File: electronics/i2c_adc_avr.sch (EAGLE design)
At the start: 17 parts, among them IC1 TINY24/44/84-MU, IC2 TINY25/45/85-20MU

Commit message: Rev 0.3 as built (version is mislabeled on silk)
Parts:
- removed IC2: TINY25/45/85-20MU, mes_avr:TINY25/45/85-20MU
- C3: value 1uF -> 0.001uF
- JP5: value (none) -> MISO
- JP6: value (none) -> RESET
- JP7: value (none) -> MCU
- JP8: value (none) -> SIG
- R4: value 10 -> 10K
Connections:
- net !RESET: no longer IC2.(PCINT5/RESET/ADC0/DW)PB5
- net A0: no longer IC2.(MISO/DO/AIN1/OC0B/OC1A/PCINT1)PB1
- net A1: no longer IC2.(PCINT4/XTAL2/CLKO/OC1B/ADC2)PB3
- net AIN: no longer IC2.(PCINT3/XTAL1/CLKI/OC1B/ADC3)PB4
- net GND: now also IC1.GNDPAD
- net SCL: no longer IC2.(SCK/USCK/SCL/ADC1/T0/INT0/PCINT2)PB2
- net SDA: no longer IC2.(MOSI/DI/SDA/AIN0/OC0A/OC1A/AREF/PCINT0)PB0
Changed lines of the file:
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@@
 <part name="P+1" library="supply1" deviceset="VCC" device=""/>
 <part name="SUPPLY1" library="supply2" deviceset="GND" device=""/>
-<part name="C3" library="rcl" deviceset="C-US" device="C0603" value="1uF"/>
+<part name="C3" library="rcl" deviceset="C-US" device="C0603" value="0.001uF"/>
 <part name="C2" library="rcl" deviceset="C-US" device="C0603" value="0.1uF"/>
-<part name="R4" library="rcl" deviceset="R-US_" device="R0603" value="10"/>
+<part name="R4" library="rcl" deviceset="R-US_" device="R0603" value="10K"/>
 <part name="FRAME1" library="mes" deviceset="LETTER_L" device=""/>
 <part name="A0" library="SparkFun" deviceset="SOLDERJUMPER_2WAY" device="S" value=" "/>
@@
 <part name="P+2" library="supply1" deviceset="VCC" device=""/>
 <part name="SUPPLY2" library="supply2" deviceset="GND" device=""/>
-<part name="JP5" library="pinhead-2" deviceset="PINHD-1X01" device="_2.54"/>
-<part name="JP6" library="pinhead-2" deviceset="PINHD-1X01" device="_2.54"/>
-<part name="JP7" library="pinhead-2" deviceset="PINHD-1X04" device="_2.54-S"/>
-<part name="JP8" library="pinhead-2" deviceset="PINHD-1X03" device="_2.00"/>
+<part name="JP5" library="pinhead-2" deviceset="PINHD-1X01" device="_2.54" value="MISO"/>
+<part name="JP6" library="pinhead-2" deviceset="PINHD-1X01" device="_2.54" value="RESET"/>
+<part name="JP7" library="pinhead-2" deviceset="PINHD-1X04" device="_2.54-S" value="MCU"/>
+<part name="JP8" library="pinhead-2" deviceset="PINHD-1X03" device="_2.00" value="SIG"/>
 <part name="SUPPLY6" library="supply2" deviceset="GND" device=""/>
-<part name="IC2" library="mes_avr" deviceset="TINY25/45/85" device="-20MU"/>
 </parts>
 <sheets>
@@
 <instances>
 <instance part="A1" gate="G$1" x="165.1" y="106.68" rot="MR180"/>
-<instance part="P+1" gate="VCC" x="63.5" y="154.94"/>
-<instance part="SUPPLY1" gate="GND" x="63.5" y="121.92"/>
+<instance part="P+1" gate="VCC" x="63.5" y="152.4"/>
+<instance part="SUPPLY1" gate="GND" x="63.5" y="127"/>
 <instance part="C3" gate="G$1" x="58.42" y="35.56"/>
 <instance part="C2" gate="G$1" x="50.8" y="139.7"/>
@@
 <instance part="JP8" gate="A" x="99.06" y="40.64"/>
 <instance part="SUPPLY6" gate="GND" x="76.2" y="20.32"/>
-<instance part="IC2" gate="1" x="187.96" y="147.32"/>
 </instances>
 <busses>
@@
 <label x="134.62" y="149.86" size="1.778" layer="95" rot="MR0"/>
 </segment>
-<segment>
-<pinref part="IC2" gate="1" pin="(PCINT3/XTAL1/CLKI/OC1B/ADC3)PB4"/>
-<wire x1="223.52" y1="152.4" x2="236.22" y2="152.4" width="0.1524" layer="91"/>
-<label x="236.22" y="152.4" size="1.778" layer="95"/>
-</segment>
 </net>
 <net name="SCL" class="0">
@@
 <pinref part="JP7" gate="A" pin="2"/>
 </segment>
-<segment>
-<pinref part="IC2" gate="1" pin="(SCK/USCK/SCL/ADC1/T0/INT0/PCINT2)PB2"/>
-<wire x1="223.52" y1="147.32" x2="236.22" y2="147.32" width="0.1524" layer="91"/>
-<label x="236.22" y="147.32" size="1.778" layer="95"/>
-</segment>
 </net>
 <net name="SDA" class="0">
@@
 <wire x1="127" y1="83.82" x2="99.06" y2="83.82" width="0.1524" layer="91"/>
 <pinref part="JP7" gate="A" pin="3"/>
-</segment>
-<segment>
-<pinref part="IC2" gate="1" pin="(MOSI/DI/SDA/AIN0/OC0A/OC1A/AREF/PCINT0)PB0"/>
-<wire x1="223.52" y1="142.24" x2="236.22" y2="142.24" width="0.1524" layer="91"/>
-<label x="236.22" y="142.24" size="1.778" layer="95"/>
 </segment>
 </net>
@@
 <wire x1="66.04" y1="144.78" x2="63.5" y2="144.78" width="0.1524" layer="91"/>
 <wire x1="63.5" y1="144.78" x2="63.5" y2="147.32" width="0.1524" layer="91"/>
-<wire x1="63.5" y1="147.32" x2="63.5" y2="152.4" width="0.1524" layer="91"/>
+<wire x1="63.5" y1="147.32" x2="63.5" y2="149.86" width="0.1524" layer="91"/>
 <junction x="63.5" y="147.32"/>
 <junction x="63.5" y="147.32"/>
@@
 <segment>
 <wire x1="66.04" y1="132.08" x2="63.5" y2="132.08" width="0.1524" layer="91"/>
-<wire x1="63.5" y1="132.08" x2="63.5" y2="129.54" width="0.1524" layer="91"/>
 <pinref part="SUPPLY1" gate="GND" pin="GND"/>
-<wire x1="63.5" y1="124.46" x2="63.5" y2="129.54" width="0.1524" layer="91"/>
-<junction x="63.5" y="129.54"/>
-<junction x="63.5" y="129.54"/>
-<wire x1="50.8" y1="129.54" x2="63.5" y2="129.54" width="0.1524" layer="91"/>
+<wire x1="63.5" y1="129.54" x2="63.5" y2="132.08" width="0.1524" layer="91"/>
+<junction x="63.5" y="132.08"/>
+<junction x="63.5" y="132.08"/>
+<wire x1="50.8" y1="132.08" x2="63.5" y2="132.08" width="0.1524" layer="91"/>
 <pinref part="C2" gate="G$1" pin="2"/>
-<wire x1="50.8" y1="134.62" x2="50.8" y2="129.54" width="0.1524" layer="91"/>
+<wire x1="50.8" y1="134.62" x2="50.8" y2="132.08" width="0.1524" layer="91"/>
 <pinref part="IC1" gate="1" pin="GND"/>
+<pinref part="IC1" gate="1" pin="GNDPAD"/>
+<wire x1="66.04" y1="137.16" x2="63.5" y2="137.16" width="0.1524" layer="91"/>
+<wire x1="63.5" y1="137.16" x2="63.5" y2="132.08" width="0.1524" layer="91"/>
 </segment>
 <segment>
@@
 <label x="134.62" y="132.08" size="1.778" layer="95" rot="MR0"/>
 </segment>
-<segment>
-<pinref part="IC2" gate="1" pin="(MISO/DO/AIN1/OC0B/OC1A/PCINT1)PB1"/>
-<wire x1="223.52" y1="144.78" x2="236.22" y2="144.78" width="0.1524" layer="91"/>
-<label x="236.22" y="144.78" size="1.778" layer="95"/>
-</segment>
 </net>
 <net name="A1" class="0">
@@
 <label x="134.62" y="134.62" size="1.778" layer="95" rot="MR0"/>
 </segment>
-<segment>
-<pinref part="IC2" gate="1" pin="(PCINT4/XTAL2/CLKO/OC1B/ADC2)PB3"/>
-<wire x1="223.52" y1="149.86" x2="236.22" y2="149.86" width="0.1524" layer="91"/>
-<label x="236.22" y="149.86" size="1.778" layer="95"/>
-</segment>
 </net>
 <net name="!RESET" class="0">
@@
 <pinref part="JP6" gate="A" pin="1"/>
 </segment>
-<segment>
-<pinref part="IC2" gate="1" pin="(PCINT5/RESET/ADC0/DW)PB5"/>
-<wire x1="223.52" y1="154.94" x2="236.22" y2="154.94" width="0.1524" layer="91"/>
-<label x="236.22" y="154.94" size="1.778" layer="95"/>
-</segment>
-</net>
+</net>

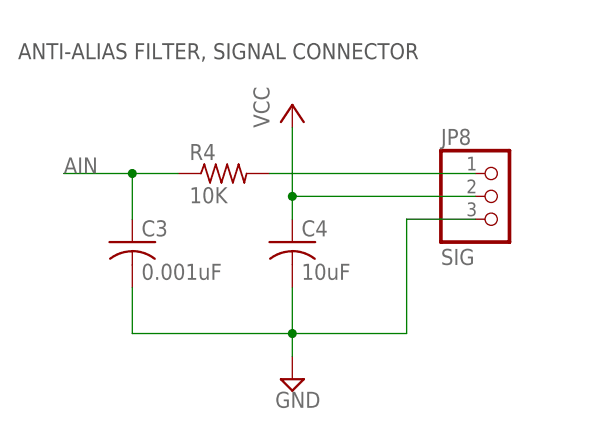
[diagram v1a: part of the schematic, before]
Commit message: Changed footprint, layout
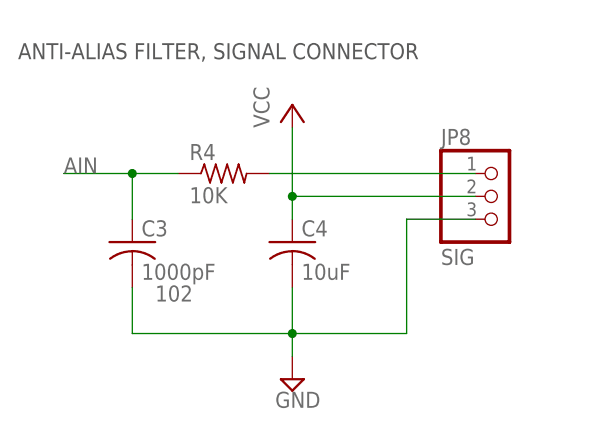
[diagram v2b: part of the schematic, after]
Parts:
- C2: PARTNO (none) -> C1608X7R1E104K080AA
- C3: value 0.001uF -> 1000pF; CODE (none) -> 102; PARTNO (none) -> CL10B102KB8SFNC
- C4: PARTNO (none) -> CL10A106MP8NNNC
- IC1: PARTNO (none) -> ATTINY44A-MU
- R0, R1, R2: PARTNO (none) -> RC1608J224CS
- R3, R4: PARTNO (none) -> 1622829-1
